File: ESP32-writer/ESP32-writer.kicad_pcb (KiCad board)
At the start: 2 copper layers, 31.2 x 30.5 mm, 18 parts, among them J1 USB2.0_C, J2 UART-OUTPUT, J3 USB2.0_C, Q1 2N7002, Q2 2N7002, U1 CH340C, U2 ESP-Prog-ProgramCOM-SEND

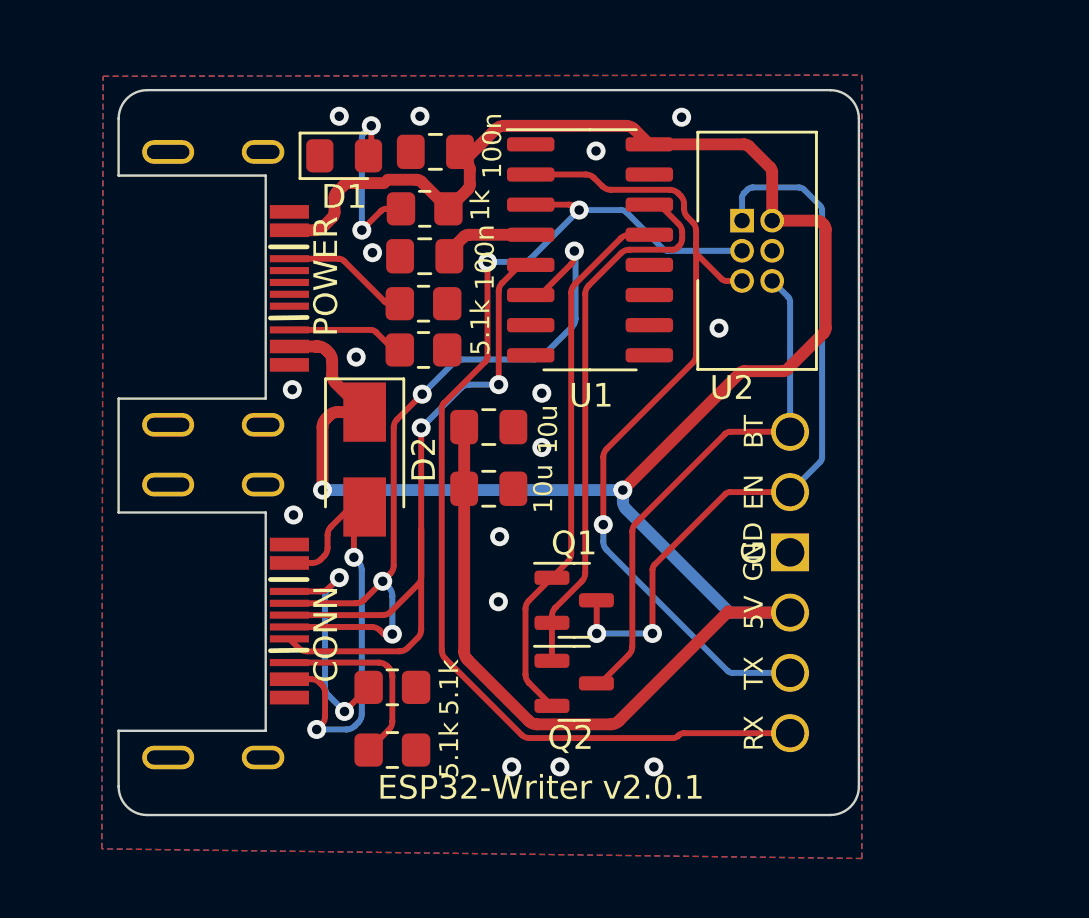
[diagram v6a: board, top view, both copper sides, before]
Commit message: replace usb type-c
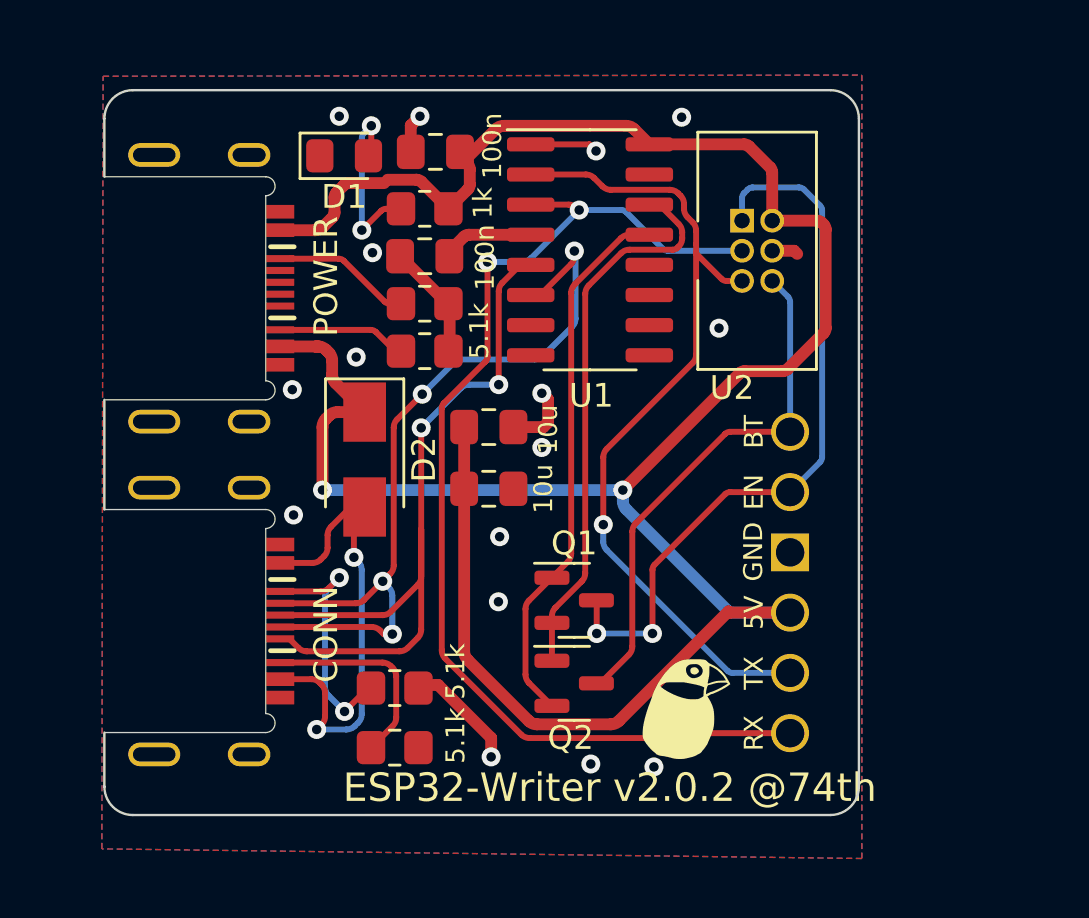
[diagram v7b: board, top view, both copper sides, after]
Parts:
- added G***: LOGO, $74th:74th-5mm, F.Cu at (90.8, 88.1)
- moved J1 7.80 mm to (66.4, 70.2)
- moved J3 7.80 mm to (66.4, 84.2)
- moved R2 0.16 mm to (79.9, 72.8)
- moved R3 0.14 mm to (79.9, 66.8)
- moved R4 0.13 mm to (78.6, 87.0)
- moved R1 0.11 mm to (79.9, 70.8)
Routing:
- net GND: track 0.07 -> 18.1 mm
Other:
- board size 31.2 x 30.5 mm -> 31.8 x 30.6 mm
- board text added: "ESP32-Writer v2.0.2 @74th"
- board text removed: "ESP32-Writer v2.0.1"
